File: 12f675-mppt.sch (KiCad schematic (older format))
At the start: 35 parts, among them IC1 PIC12F629-I/P, Q1 BUK9511-55A127, Q2 BUK9511-55A127, Q3 2N2222A, Q4 2N2222A, Q5 2N2907A, U1 7805, U2 LM358N

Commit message: Circuit design changes. more sensivity on current measuring adc.
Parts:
- added R1: 10k, symbol R
- added R15: 100k, symbol R
- added unit 1 of U2
- U2: symbol LM358N -> LM358N-RESCUE-12f675-mppt
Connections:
- wire segments 83 -> 93
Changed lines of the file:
@@
 EESchema Schematic File Version 2
+LIBS:12f675-mppt-rescue
 LIBS:power
 LIBS:device
@@
 $EndComp
 $Comp
-L LM358N U2
+L LM358N-RESCUE-12f675-mppt U2
 U 2 1 55C3383E
 P 7500 4850
@@
 	2650 4000 3850 4000
 Wire Wire Line
-	2650 5600 2650 3700
+	2650 3700 2650 5600
 Connection ~ 2650 4000
 Wire Wire Line
@@
 Wire Wire Line
 	7200 4250 8000 4250
-Wire Wire Line
-	8000 3600 8000 4850
-Connection ~ 8000 4250
 Wire Wire Line
 	7000 4950 6900 4950
@@
 Heat Sink
 Wire Notes Line
-	9400 5850 9400 3750
-Wire Notes Line
-	5900 5850 9400 5850
+	5900 5850 9800 5850
 $Comp
 L R R11
@@
 $EndComp
 Wire Wire Line
-	6550 3600 8000 3600
-Wire Wire Line
 	5250 3600 6250 3600
 $Comp
@@
 	6500 3500 6700 3750
 Wire Notes Line
-	6700 3750 9400 3750
+	6700 3750 9800 3750
 $Comp
 L CP C6
@@
 	3500 6100 8150 6100
 Wire Wire Line
-	8150 6100 8150 4450
+	8150 4450 8150 6100
 Wire Wire Line
 	5250 3900 5250 4300
@@
 Connection ~ 5500 4500
 Wire Wire Line
-	6000 4450 8150 4450
-Wire Wire Line
-	1600 5600 8400 5600
+	6000 4450 8450 4450
+Wire Wire Line
+	9450 5600 1600 5600
 Text Label 8550 6000 0    60   ~ 0
 3.6v
+$Comp
+L LM358N-RESCUE-12f675-mppt U2
+U 1 1 56E669E2
+P 8850 4350
+F 0 "U2" H 8800 4550 60  0000 L CNN
+F 1 "LM358N" H 8800 4100 60  0000 L CNN
+F 2 "" H 8850 4350 60  0000 C CNN
+F 3 "" H 8850 4350 60  0000 C CNN
+	1    8850 4350
+	0    -1   -1   0
+$EndComp
+Wire Wire Line
+	8000 4250 8000 4850
+Wire Wire Line
+	8000 4850 8750 4850
+Wire Wire Line
+	8850 3850 8850 3600
+Wire Wire Line
+	6550 3600 9650 3600
+$Comp
+L R R1
+U 1 1 56E67518
+P 9200 4850
+F 0 "R1" V 9280 4850 50  0000 C CNN
+F 1 "10k" V 9200 4850 50  0000 C CNN
+F 2 "" V 9130 4850 50  0000 C CNN
+F 3 "" H 9200 4850 50  0000 C CNN
+	1    9200 4850
+	0    1    1    0
+$EndComp
+Wire Wire Line
+	9450 4450 9450 5600
+Connection ~ 8400 5600
+Wire Wire Line
+	9050 4850 8950 4850
+Wire Wire Line
+	9450 4450 9250 4450
+Connection ~ 9450 4850
+Connection ~ 8150 4450
+$Comp
+L R R15
+U 1 1 56E68956
+P 9650 4300
+F 0 "R15" V 9730 4300 50  0000 C CNN
+F 1 "100k" V 9650 4300 50  0000 C CNN
+F 2 "" V 9580 4300 50  0000 C CNN
+F 3 "" H 9650 4300 50  0000 C CNN
+	1    9650 4300
+	-1   0    0    1
+$EndComp
+Wire Wire Line
+	9650 5100 9650 4450
+Wire Wire Line
+	9650 3600 9650 4150
+Connection ~ 8850 3600
+Wire Notes Line
+	9800 3750 9800 5850
+Wire Wire Line
+	9350 4850 9450 4850
+Wire Wire Line
+	9650 5100 8950 5100
+Wire Wire Line
+	8950 5100 8950 4850
 $EndSCHEMATC

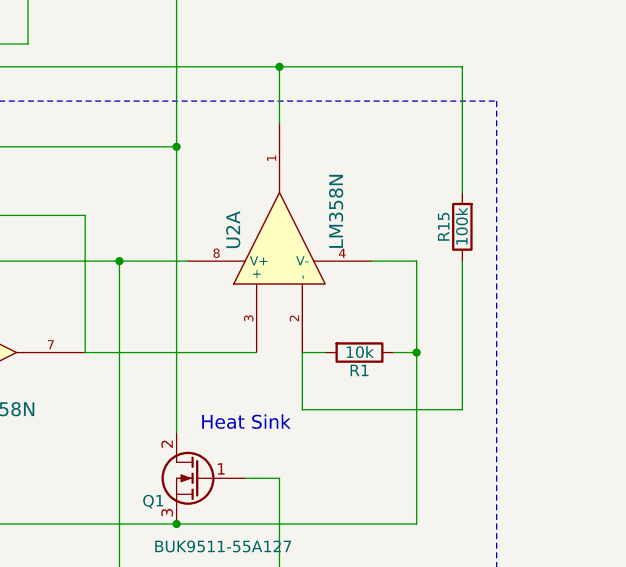
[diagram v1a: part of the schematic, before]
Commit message: circuit v3. reduce op-amp amplification.
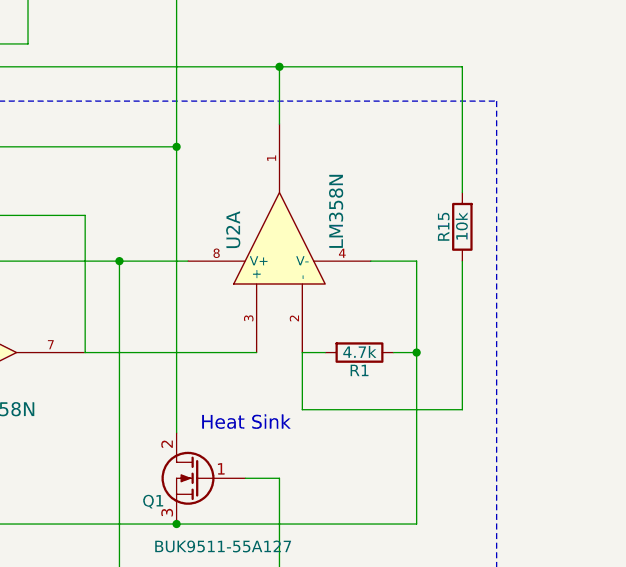
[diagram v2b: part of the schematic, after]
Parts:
- R1: value 10k -> 4.7k
- R15: value 100k -> 10k
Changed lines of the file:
@@
 encoding utf-8
 Sheet 1 1
-Title "Simple MPPT with 12F675"
-Date "2015-08-30"
-Rev "1.1h"
+Title "Simple MPPT with 12F675 v3"
+Date "2016-03-14"
+Rev "1.3"
 Comp ""
 Comment1 ""
@@
 P 9200 4850
 F 0 "R1" V 9280 4850 50  0000 C CNN
-F 1 "10k" V 9200 4850 50  0000 C CNN
+F 1 "4.7k" V 9200 4850 50  0000 C CNN
 F 2 "" V 9130 4850 50  0000 C CNN
 F 3 "" H 9200 4850 50  0000 C CNN
@@
 P 9650 4300
 F 0 "R15" V 9730 4300 50  0000 C CNN
-F 1 "100k" V 9650 4300 50  0000 C CNN
+F 1 "10k" V 9650 4300 50  0000 C CNN
 F 2 "" V 9580 4300 50  0000 C CNN
 F 3 "" H 9650 4300 50  0000 C CNN

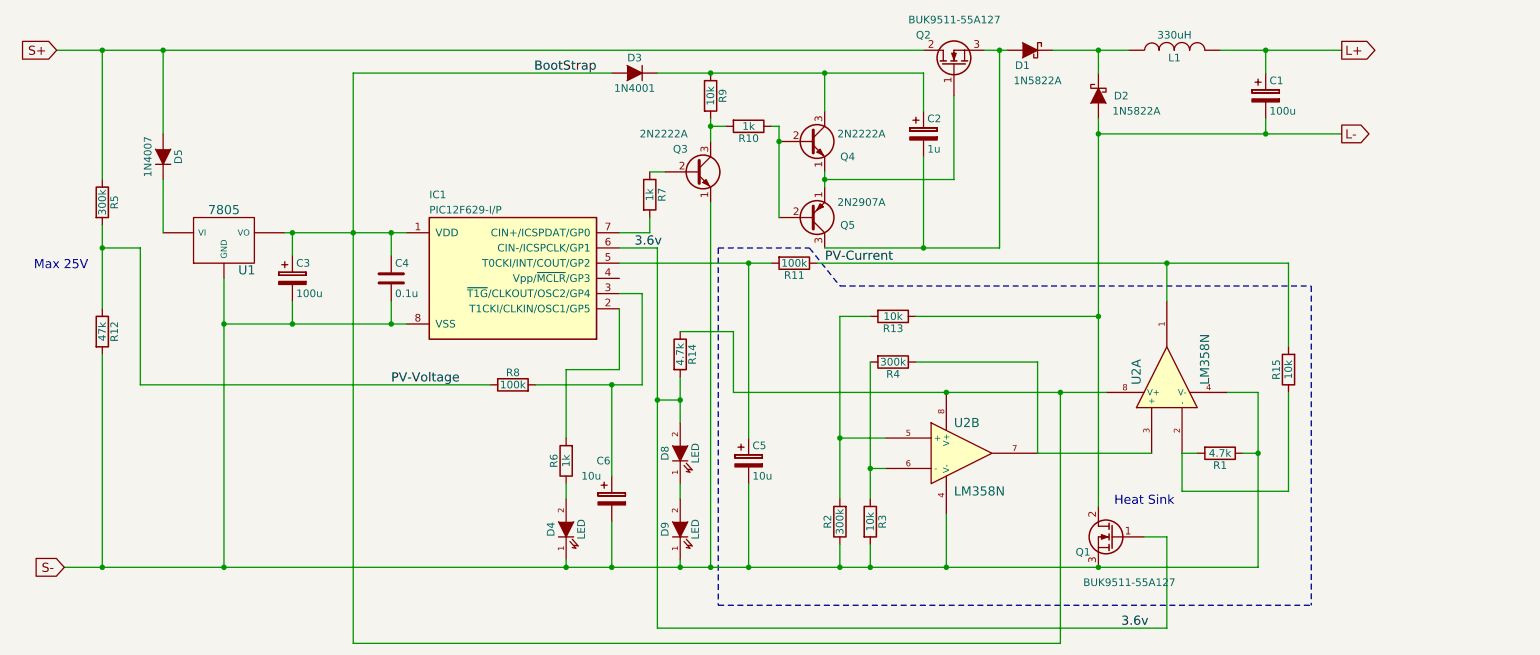
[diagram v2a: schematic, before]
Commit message: Add switch for OP-AMP calibration support. Push on this at no load and OP-AMP offset value write on eeprom.
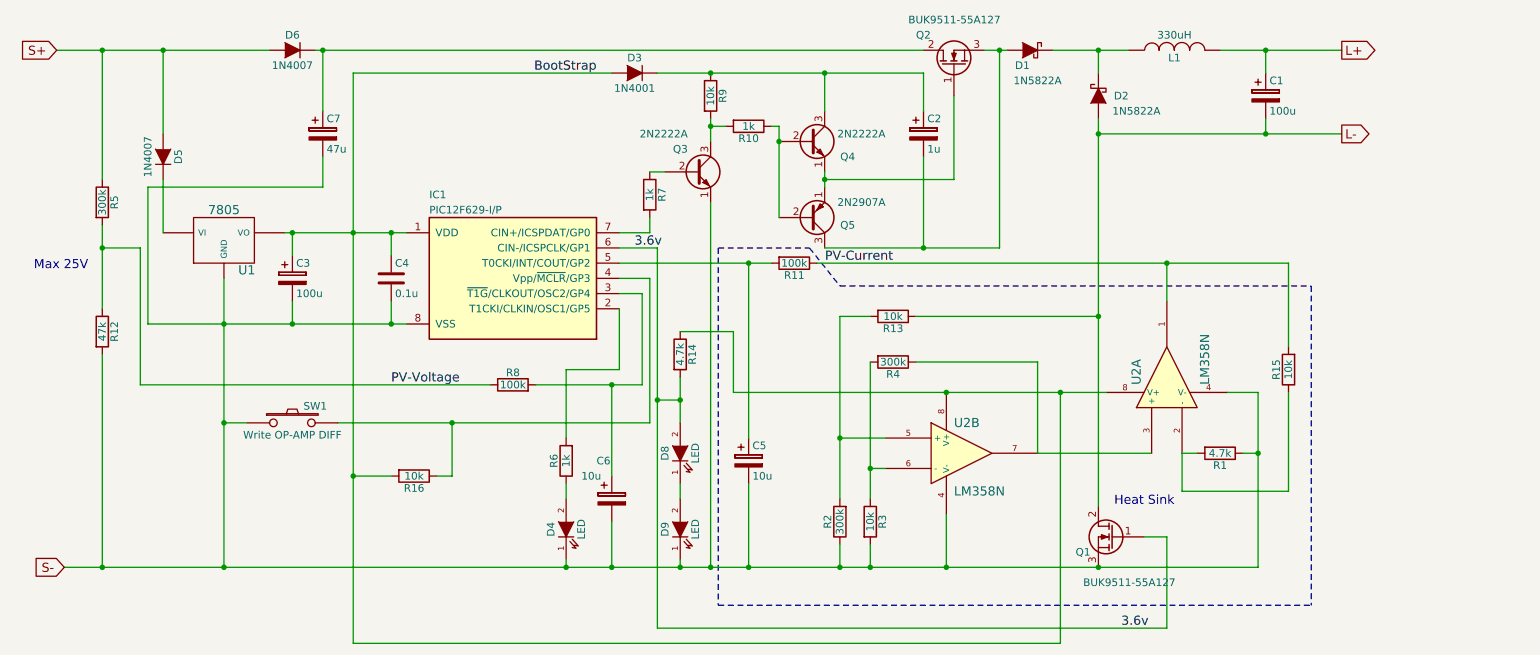
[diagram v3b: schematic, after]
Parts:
- added C7: 47u, symbol CP
- added D6: 1N4007, symbol D
- added R16: 10k, symbol R
- added SW1: Write OP-AMP DIFF, symbol SW_PUSH
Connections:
- net BootStrap: now also R16.2
- net S+: now also D6.2 (A); no longer Q2.2 (D)
- net S-: now also C7.2, SW1.1
- net at IC1.4 (Vpp/~MCLR~/GP3): now also R16.1, SW1.2
- new net: C7.1, D6.1 (K), Q2.2 (D)

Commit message: update capacitor and diode.
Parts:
- C1, C3, C5, C6, C7: symbol CP -> Device:CP
- C2: value 1u -> 10u 50v; symbol CP -> Device:CP
- C4: symbol C -> Device:C
- D1, D2: symbol D_Schottky -> Device:D_Schottky
- D3: value 1N4001 -> 1N4148; symbol D -> Device:D
- D4, D8, D9: symbol LED -> 12f675-mppt-rescue:LED
- D5, D6: symbol D -> Device:D
- IC1: symbol PIC12F629-I/P -> 12f675-mppt-rescue:PIC12F629-I_P
- L1: symbol INDUCTOR -> 12f675-mppt-rescue:INDUCTOR
- Q1, Q2: symbol Q_NMOS_GDS -> Device:Q_NMOS_GDS
- Q3, Q4: symbol Q_NPN_EBC -> Device:Q_NPN_EBC
- Q5: symbol Q_PNP_EBC -> Device:Q_PNP_EBC
- R1, R10, R11, R12, R13, R14, R15, R16, R2, R3, R4, R5, R6, R7, R8, R9: symbol R -> Device:R
- SW1: symbol SW_PUSH -> 12f675-mppt-rescue:SW_PUSH
- U1: symbol 7805 -> 12f675-mppt-rescue:7805
- U2: symbol LM358N-RESCUE-12f675-mppt -> 12f675-mppt-rescue:LM358N-RESCUE-12f675-mppt

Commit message: Remove R11. It's a lot lower current sensing voltage.
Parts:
- removed R11: 100k, symbol Device:R
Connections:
- net PV-Current: now also C5.1, IC1.5 (T0CKI/INT/COUT/GP2)
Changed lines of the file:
@@
 Sheet 1 1
 Title "Simple MPPT with 12F675 v4"
-Date "2016-03-19"
-Rev "1.4"
+Date "2018-11-30"
+Rev "1.5"
 Comp ""
 Comment1 ""
@@
 Heat Sink
 $Comp
-L Device:R R11
-U 1 1 55C4C21C
-P 6400 3600
-F 0 "R11" V 6480 3600 50  0000 C CNN
-F 1 "100k" V 6400 3600 50  0000 C CNN
-F 2 "" V 6330 3600 30  0000 C CNN
-F 3 "" H 6400 3600 30  0000 C CNN
-	1    6400 3600
-	0    1    1    0
-$EndComp
-$Comp
 L Device:R R12
 U 1 1 55C48C57
@@
 	8850 3850 8850 3600
 Wire Wire Line
-	6550 3600 8850 3600
-Wire Wire Line
 	9450 4450 9450 4850
 Connection ~ 8400 5600
@@
 	6100 5600 5850 5600
 Wire Wire Line
-	6100 3600 6250 3600
-Wire Wire Line
 	5200 5600 4900 5600
 Wire Wire Line
@@
 Wire Wire Line
 	2650 4650 2650 5600
+Wire Wire Line
+	6100 3600 8850 3600
 $EndSCHEMATC

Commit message: Remove C6.
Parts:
- removed C6: 10u, symbol Device:CP
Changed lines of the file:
@@
 Sheet 1 1
 Title "Simple MPPT with 12F675 v4"
-Date "2018-11-30"
-Rev "1.5"
+Date "2018-12-17"
+Rev "1.6"
 Comp ""
 Comment1 ""
@@
 	1    0    0    -1
 $EndComp
-$Comp
-L Device:CP C6
-U 1 1 55D02AF9
-P 5200 5150
-F 0 "C6" H 5100 5400 50  0000 L CNN
-F 1 "10u" H 5000 5300 50  0000 L CNN
-F 2 "" H 5238 5000 30  0000 C CNN
-F 3 "" H 5200 5150 60  0000 C CNN
-	1    5200 5150
-	1    0    0    -1
-$EndComp
 Text Label 8550 6000 0    60   ~ 0
 3.6v
@@
 	4900 4300 4900 4750
 Wire Wire Line
-	5200 5300 5200 5600
-Connection ~ 5200 5600
-Wire Wire Line
 	2100 3500 2100 4400
 Wire Wire Line
 	2100 4400 4400 4400
 Wire Wire Line
-	4700 4400 5200 4400
-Wire Wire Line
 	5400 4400 5400 3800
 Wire Wire Line
 	5400 3800 5250 3800
-Wire Wire Line
-	5200 5000 5200 4400
-Connection ~ 5200 4400
 Wire Wire Line
 	5650 4500 5500 4500
@@
 	8400 3950 8400 5200
 Wire Wire Line
-	5650 5600 5200 5600
-Wire Wire Line
 	6100 5600 5850 5600
 Wire Wire Line
-	5200 5600 4900 5600
-Wire Wire Line
-	5200 4400 5400 4400
-Wire Wire Line
 	5650 4500 5650 4650
 Wire Wire Line
@@
 Wire Wire Line
 	6100 3600 8850 3600
+Wire Wire Line
+	4700 4400 5400 4400
+Wire Wire Line
+	4900 5600 5650 5600
 $EndSCHEMATC

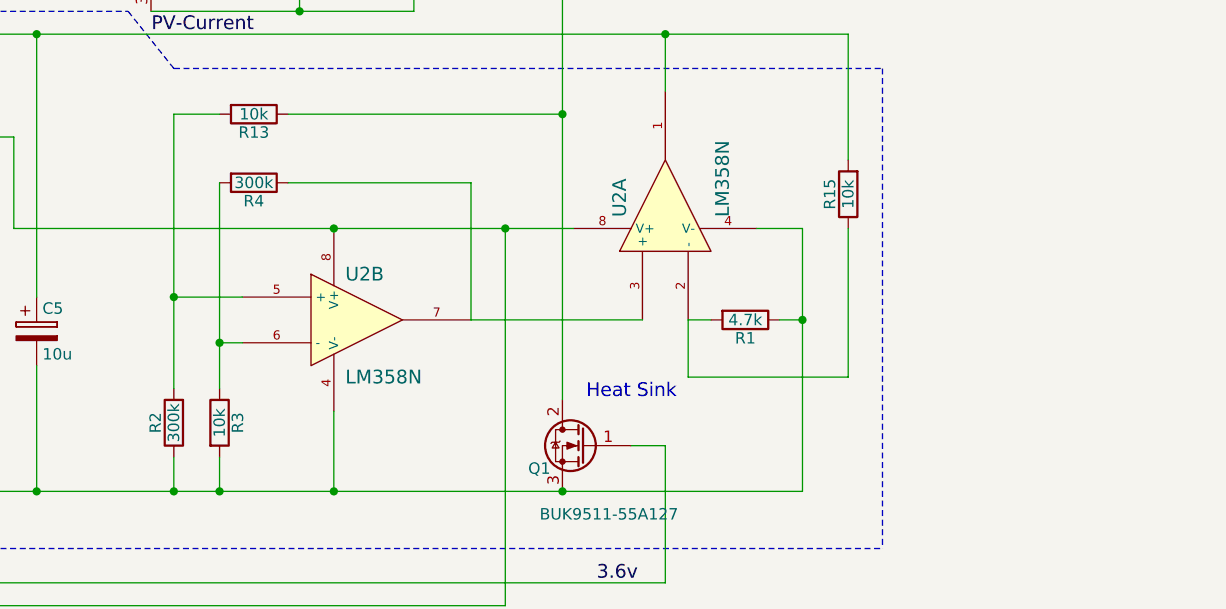
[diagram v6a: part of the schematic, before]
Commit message: Fix R2, R4 value. 300k -> 100k. Add R15 hint.
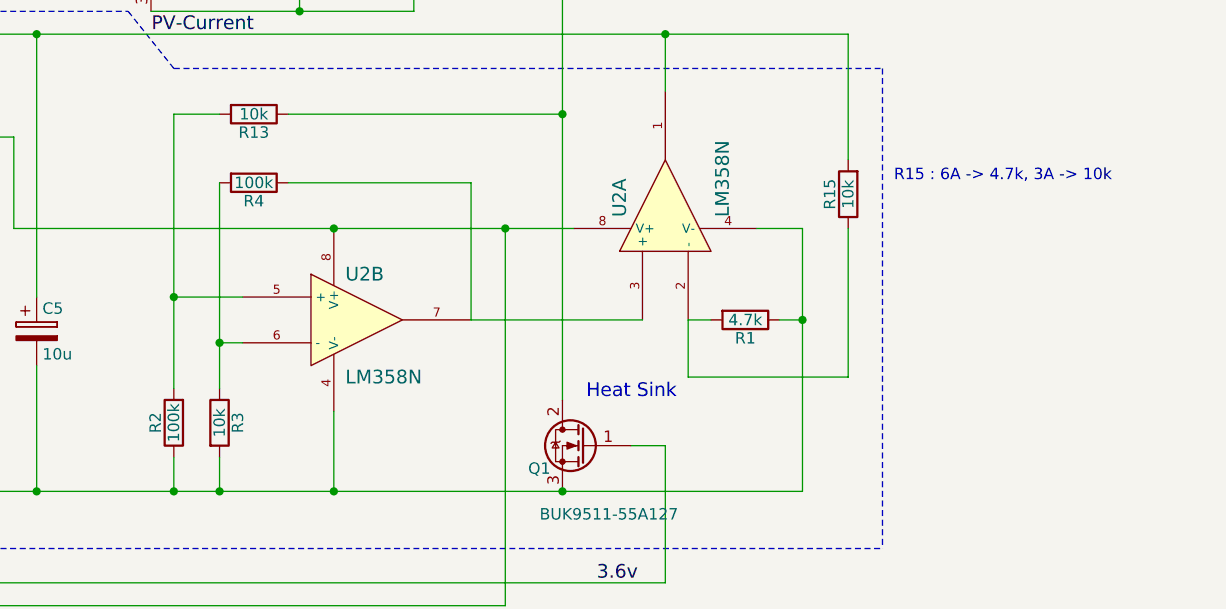
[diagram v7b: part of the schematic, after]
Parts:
- R2, R4: value 300k -> 100k
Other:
- note added: "R15 : 6A -> 4.7k, 3A -> 10k"
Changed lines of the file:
@@
 Sheet 1 1
 Title "Simple MPPT with 12F675 v4"
-Date "2018-12-17"
-Rev "1.6"
+Date "2019-01-11"
+Rev "1.6a"
 Comp ""
 Comment1 ""
@@
 P 7050 4250
 F 0 "R4" V 7130 4250 50  0000 C CNN
-F 1 "300k" V 7050 4250 50  0000 C CNN
+F 1 "100k" V 7050 4250 50  0000 C CNN
 F 2 "" V 6980 4250 30  0000 C CNN
 F 3 "" H 7050 4250 30  0000 C CNN
@@
 P 6700 5300
 F 0 "R2" V 6780 5300 50  0000 C CNN
-F 1 "300k" V 6700 5300 50  0000 C CNN
+F 1 "100k" V 6700 5300 50  0000 C CNN
 F 2 "" V 6630 5300 30  0000 C CNN
 F 3 "" H 6700 5300 30  0000 C CNN
@@
 Wire Wire Line
 	4900 5600 5650 5600
+Text Notes 9850 4250 0    50   ~ 0
+R15 : 6A -> 4.7k, 3A -> 10k
 $EndSCHEMATC

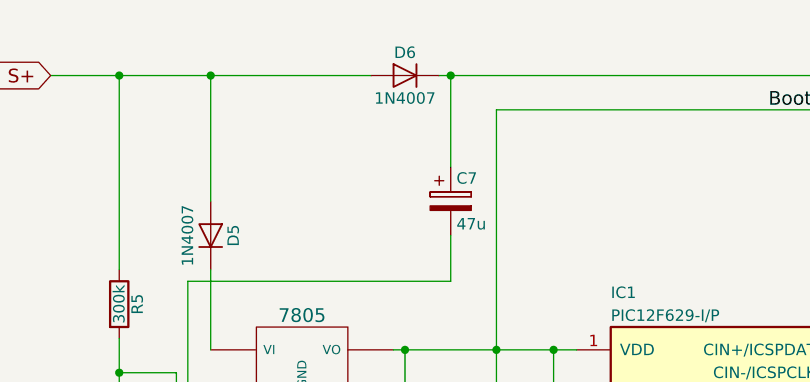
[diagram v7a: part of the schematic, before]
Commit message: Fix D6 value.
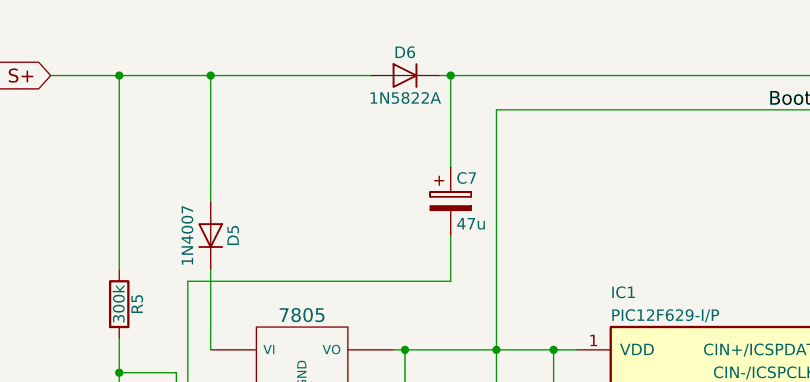
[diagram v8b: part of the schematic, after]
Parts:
- D6: value 1N4007 -> 1N5822A
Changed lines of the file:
@@
 encoding utf-8
 Sheet 1 1
-Title "Simple MPPT with 12F675 v4"
+Title "Simple MPPT with 12F675 v5"
 Date "2019-01-11"
-Rev "1.6a"
+Rev "1.6b"
 Comp ""
 Comment1 ""
@@
 P 3100 2200
 F 0 "D6" H 3100 2300 50  0000 C CNN
-F 1 "1N4007" H 3100 2100 50  0000 C CNN
+F 1 "1N5822A" H 3100 2100 50  0000 C CNN
 F 2 "" H 3100 2200 60  0000 C CNN
 F 3 "" H 3100 2200 60  0000 C CNN
